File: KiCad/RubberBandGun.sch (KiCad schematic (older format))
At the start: 19 parts

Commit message: wiring for solenoid & move to pin 8
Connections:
- wire segments 120 -> 124
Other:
- note added: "Barrel Black Gnd\n Solenoid"
- note added: "Barrel White +5V\n Solenoid"
- note added: "D08 = Barrel (Yellow)\n grounded = closed"
- note added: "D13 = Solenoid\n (Blue)"
- note removed: "D09 = Barrel\n grounded = closed"
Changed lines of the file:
@@
 D07 = Red
 Text Notes 2200 2900 0    59   ~ 0
-D09 = Barrel\n    grounded = closed
+D08 = Barrel (Yellow)\n    grounded = closed
 $Comp
 L switches:SW_SPST SW?
@@
 	0    -1   -1   0
 $EndComp
-Text Notes 4850 5600 0    59   ~ 0
-D09 = Barrel\n    grounded = closed
+Text Notes 7250 4200 0    59   ~ 0
+Barrel White +5V\n    Solenoid
 $Comp
 L mdoLibrary:YX5200 A?
@@
 	4400 1100 4400 950
 Connection ~ 4400 950
-Wire Wire Line
-	4400 1400 4400 2800
 Wire Notes Line
 	7650 4450 7650 4750
@@
 Wire Wire Line
 	5350 3700 5350 3100
-Wire Wire Line
-	5350 2800 4400 2800
-Connection ~ 4400 2800
 Connection ~ 4200 6400
 Wire Wire Line
@@
 	7400 4500 7650 4500
 Wire Wire Line
-	7650 4500 7650 4700
+	7650 4500 7650 4600
 Wire Wire Line
 	7650 4700 7400 4700
@@
 Wire Wire Line
 	7050 6400 4800 6400
-Wire Wire Line
-	4400 2800 4400 4500
 Wire Wire Line
 	4200 6400 4000 6400
@@
 	1    0    0    -1
 $EndComp
+Wire Wire Line
+	4400 1400 4400 2700
+Wire Wire Line
+	5350 2700 4400 2700
+Connection ~ 4400 2700
+Wire Wire Line
+	4400 2700 4400 4500
+Text Notes 6600 3100 0    59   ~ 0
+D13 = Solenoid\n   (Blue)
+Text Notes 7250 5850 0    59   ~ 0
+Barrel Black Gnd\n    Solenoid
+Wire Wire Line
+	6550 3100 7200 3100
+Wire Wire Line
+	7200 3100 7200 4600
+Wire Wire Line
+	7200 4600 7650 4600
+Connection ~ 7650 4600
+Wire Wire Line
+	7650 4600 7650 4700
 $EndSCHEMATC

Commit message: latest schematic updates
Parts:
- added R?: 1.6K, symbol Device:R
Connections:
- wire segments 124 -> 128
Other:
- note added: "Barrel White +7.4V\n Solenoid"
- note added: "USB Breakout\n Black - GND\n White - +7.4 V\n Blue - Trig (HI = active)\n Yellow - Sense (GND = cnct)"
- note added: "Yes - connect GND"
- note removed: "Barrel White +5V\n Solenoid"
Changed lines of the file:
@@
 Sheet 1 2
 Title "FOOF Rubber Band Gun"
-Date "2020-01-30"
+Date "2020-03-14"
 Rev "---"
 Comp ""
@@
 F 3 "" H 2050 4450 60  0001 C CNN
 	1    2050 4450
-	1    0    0    -1
-$EndComp
-$Comp
-L mdoLibrary:UBEC #J0102
-U 1 1 5A459D02
-P 2050 6250
-F 0 "#J0102" H 2050 6250 60  0000 C CNN
-F 1 "UBEC" H 2050 6350 60  0000 C CNN
-F 2 "" H 2050 6250 60  0001 C CNN
-F 3 "" H 2050 6250 60  0001 C CNN
-	1    2050 6250
-	1    0    0    -1
-$EndComp
-$Comp
-L power:GND #PWR0103
-U 1 1 5A45A4D2
-P 1250 6950
-F 0 "#PWR0103" H 1250 6700 50  0001 C CNN
-F 1 "GND" H 1250 6800 50  0000 C CNN
-F 2 "" H 1250 6950 50  0001 C CNN
-F 3 "" H 1250 6950 50  0001 C CNN
-	1    1250 6950
-	1    0    0    -1
-$EndComp
-$Comp
-L power:+12V #PWR0104
-U 1 1 5A45A52D
-P 1250 5550
-F 0 "#PWR0104" H 1250 5400 50  0001 C CNN
-F 1 "+12V" H 1250 5690 50  0000 C CNN
-F 2 "" H 1250 5550 50  0001 C CNN
-F 3 "" H 1250 5550 50  0001 C CNN
-	1    1250 5550
 	1    0    0    -1
 $EndComp
@@
 Text Notes 7950 4850 3    118  ~ 0
 solenoid\ndriver
-Text Notes 900  3500 0    118  ~ 0
+Text Notes 1450 3850 0    118  ~ 0
 7.4 Volts
 $Comp
@@
 	0    -1   -1   0
 $EndComp
-Text Notes 7250 4200 0    59   ~ 0
-Barrel White +5V\n    Solenoid
+Text Notes 7450 4150 0    59   ~ 0
+Barrel White +7.4V\n    Solenoid
 $Comp
 L mdoLibrary:YX5200 A?
@@
 	1    0    0    -1
 $EndComp
-Connection ~ 3050 6400
-Wire Wire Line
-	1250 6000 1250 5550
-Wire Wire Line
-	1550 6000 1250 6000
-Wire Wire Line
-	1250 6400 1250 6950
-Wire Wire Line
-	1550 6400 1250 6400
 Wire Wire Line
 	9850 6400 8150 6400
 Wire Wire Line
-	3050 4600 3050 6400
+	3050 4600 3050 4900
 Wire Wire Line
 	2750 4600 3050 4600
@@
 	1250 4200 1550 4200
 Wire Wire Line
-	1250 3850 1250 4200
+	1250 3850 1250 3950
 Wire Wire Line
 	1250 4600 1550 4600
 Wire Wire Line
-	1250 4950 1250 4600
+	1250 4950 1250 4900
 Wire Wire Line
 	3200 4200 2750 4200
@@
 Connection ~ 4000 2500
 Wire Wire Line
-	2750 6000 9950 6000
-Wire Wire Line
 	9950 6000 9950 1800
 Wire Wire Line
-	6550 2000 7400 2000
-Connection ~ 7400 2000
+	6550 2000 6950 2000
 Wire Wire Line
 	4200 1100 4200 950
@@
 	4750 3900 4750 950
 Connection ~ 4750 950
-Wire Wire Line
-	7400 950  7400 2000
 Connection ~ 4600 950
 Wire Wire Line
@@
 Wire Wire Line
 	4600 1400 7600 1400
-Connection ~ 7400 950
 Wire Wire Line
 	7850 2150 7600 2150
@@
 	9350 1500 4950 1500
 Wire Wire Line
-	3050 6400 2750 6400
-Wire Wire Line
 	3400 6400 3050 6400
 Wire Wire Line
@@
 	4000 2500 4000 4100
 Wire Wire Line
-	7400 2000 7400 4500
-Wire Wire Line
 	4200 950  4400 950
 Wire Wire Line
@@
 	4800 6400 4200 6400
 Wire Wire Line
-	4750 950  7400 950
+	4750 950  6950 950
 Wire Wire Line
 	4600 950  4750 950
@@
 Wire Wire Line
 	7600 2250 7600 2450
-Wire Wire Line
-	7400 950  9050 950
 Wire Wire Line
 	9200 2250 9200 2350
@@
 	6550 3100 7200 3100
 Wire Wire Line
-	7200 3100 7200 4600
-Wire Wire Line
 	7200 4600 7650 4600
 Connection ~ 7650 4600
 Wire Wire Line
 	7650 4600 7650 4700
+Wire Wire Line
+	7200 3100 7200 3300
+Wire Wire Line
+	7200 3600 7200 4600
+$Comp
+L Device:R R?
+U 1 1 5E6E688B
+P 7200 3450
+F 0 "R?" V 7280 3450 50  0000 C CNN
+F 1 "1.6K" V 7200 3450 50  0000 C CNN
+F 2 "" V 7130 3450 50  0001 C CNN
+F 3 "" H 7200 3450 50  0001 C CNN
+	1    7200 3450
+	1    0    0    -1
+$EndComp
+Wire Wire Line
+	3200 4200 3200 6000
+Connection ~ 3200 4200
+Wire Wire Line
+	3200 6000 9950 6000
+Wire Wire Line
+	1250 4900 3050 4900
+Connection ~ 1250 4900
+Wire Wire Line
+	1250 4900 1250 4600
+Connection ~ 3050 4900
+Wire Wire Line
+	3050 4900 3050 6400
+Text Notes 1750 5000 0    59   ~ 0
+Yes - connect GND
+Wire Wire Line
+	6950 950  6950 2000
+Connection ~ 6950 950
+Wire Wire Line
+	6950 950  9050 950
+Wire Wire Line
+	1250 3950 1400 3950
+Wire Wire Line
+	1400 3950 1400 750
+Wire Wire Line
+	1400 750  7400 750
+Wire Wire Line
+	7400 750  7400 4500
+Connection ~ 1250 3950
+Wire Wire Line
+	1250 3950 1250 4200
+Text Notes 8300 4800 0    59   ~ 0
+USB Breakout\n   Black - GND\n   White - +7.4 V\n   Blue - Trig (HI = active)\n   Yellow - Sense (GND = cnct)
 $EndSCHEMATC

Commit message: add solenoid circuit
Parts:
- removed L?: L, symbol Device:L
- removed R?: 10K, symbol Device:R
- removed SW?: SW_SPST, symbol switches:SW_SPST
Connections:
- net labels added: Black, Blue, White, Yellow
- wire segments 128 -> 106
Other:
- note removed: "Barrel Black Gnd\n Solenoid"
- note removed: "Barrel White +7.4V\n Solenoid"
- note removed: "USB Breakout\n Black - GND\n White - +7.4 V\n Blue - Trig (HI = active)\n Yellow - Sense (GND = cnct)"
- note removed: "solenoid\ndriver"

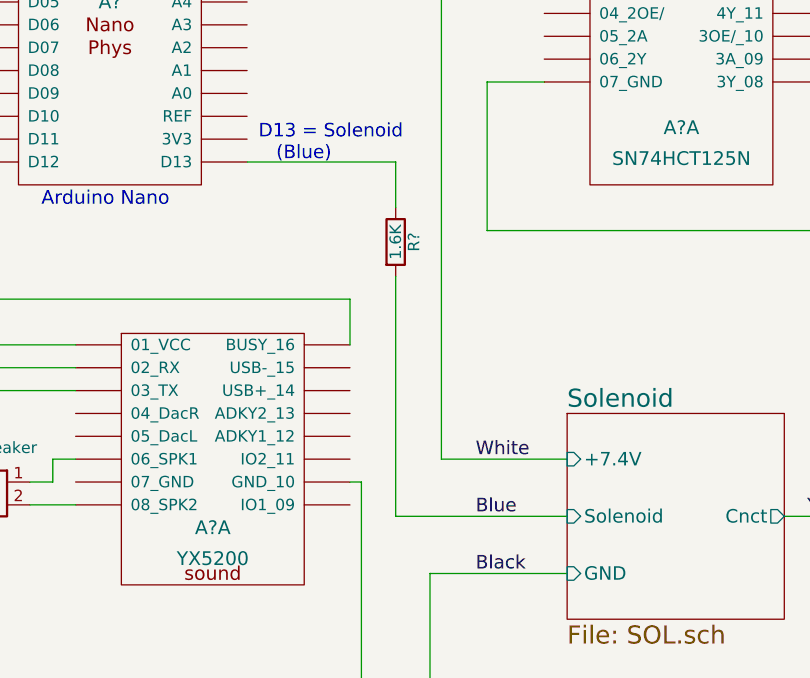
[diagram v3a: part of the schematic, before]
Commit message: small change to schematic
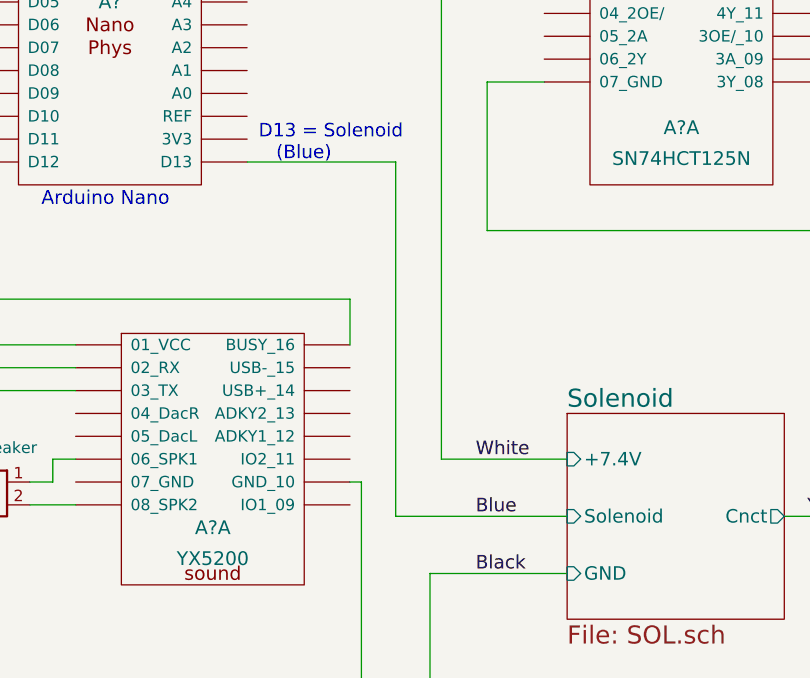
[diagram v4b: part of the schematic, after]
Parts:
- removed R?: 1.6K, symbol Device:R
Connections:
- wire segments 106 -> 105
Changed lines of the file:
@@
 Sheet 1 2
 Title "FOOF Rubber Band Gun"
-Date "2020-03-14"
+Date "2020-04-02"
 Rev "---"
 Comp ""
@@
 Wire Wire Line
 	6550 3100 7200 3100
-Wire Wire Line
-	7200 3100 7200 3300
-$Comp
-L Device:R R?
-U 1 1 5E6E688B
-P 7200 3450
-F 0 "R?" V 7280 3450 50  0000 C CNN
-F 1 "1.6K" V 7200 3450 50  0000 C CNN
-F 2 "" V 7130 3450 50  0001 C CNN
-F 3 "" H 7200 3450 50  0001 C CNN
-	1    7200 3450
-	1    0    0    -1
-$EndComp
 Wire Wire Line
 	3200 4200 3200 6000
@@
 $EndSheet
 Wire Wire Line
-	7200 3600 7200 4650
-Wire Wire Line
 	4200 6400 7050 6400
 Wire Wire Line
@@
 Wire Wire Line
 	4400 950  4750 950
+Wire Wire Line
+	7200 3100 7200 4650
 $EndSCHEMATC

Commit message: update schematic to show power and USB details
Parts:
- added SW?: ToggleSW, symbol switches:SW_SPST
- added U?: SolenoidDriver, symbol mdoLibrary:SolenoidDriver
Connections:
- net labels added: +8V
- net labels removed: +12V, Black, Blue, White, Yellow
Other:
- note added: "8.3 Volts"
- note added: "Black"
- note added: "Blue"
- note added: "White"
- note added: "Yellow"
- note removed: "7.4 Volts"
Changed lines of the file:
@@
 $Descr A 11000 8500
 encoding utf-8
-Sheet 1 2
+Sheet 1 1
 Title "FOOF Rubber Band Gun"
-Date "2020-04-02"
+Date "2020-07-13"
 Rev "---"
 Comp ""
@@
 Comment4 ""
 $EndDescr
-$Comp
-L power:+12V #PWR0101
-U 1 1 5A3DEBB7
-P 1250 3850
-F 0 "#PWR0101" H 1250 3700 50  0001 C CNN
-F 1 "+12V" H 1250 3990 50  0000 C CNN
-F 2 "" H 1250 3850 50  0001 C CNN
-F 3 "" H 1250 3850 50  0001 C CNN
-	1    1250 3850
-	1    0    0    -1
-$EndComp
 $Comp
 L power:GND #PWR0102
@@
 $EndComp
 Text Notes 1450 3850 0    118  ~ 0
-7.4 Volts
+8.3 Volts
 $Comp
 L Device:R R?
@@
 	2750 4600 3050 4600
 Wire Wire Line
-	1250 4200 1550 4200
-Wire Wire Line
-	1250 3850 1250 3950
-Wire Wire Line
 	1250 4600 1550 4600
 Wire Wire Line
@@
 	6950 950  9050 950
 Wire Wire Line
-	1250 3950 1400 3950
-Wire Wire Line
-	1400 3950 1400 750
-Wire Wire Line
 	1400 750  7400 750
 Wire Wire Line
-	7400 750  7400 4400
-Connection ~ 1250 3950
-Wire Wire Line
-	1250 3950 1250 4200
-Text Label 7550 4400 0    59   ~ 0
-White
-$Sheet
-S 7950 4200 950  900
-U 5B063CC5
-F0 "Solenoid" 79
-F1 "SOL.sch" 79
-F2 "+7.4V" I L 7950 4400 59
-F3 "GND" I L 7950 4900 59
-F4 "Solenoid" I L 7950 4650 59
-F5 "Cnct" O R 8900 4650 59
-$EndSheet
+	7400 750  7400 4300
 Wire Wire Line
 	4200 6400 7050 6400
 Wire Wire Line
-	7050 6400 7350 6400
-Wire Wire Line
-	7400 4400 7950 4400
-Wire Wire Line
-	7200 4650 7950 4650
-Wire Wire Line
-	7350 6400 7350 4900
-Wire Wire Line
-	7350 4900 7950 4900
-Connection ~ 7350 6400
-Wire Wire Line
-	7350 6400 9850 6400
-Wire Wire Line
-	4400 5500 9750 5500
-Wire Wire Line
-	9750 5500 9750 4650
-Wire Wire Line
 	4400 2700 4400 5500
-Wire Wire Line
-	8900 4650 9750 4650
-Text Label 7550 4900 0    59   ~ 0
-Black
-Text Label 7550 4650 0    59   ~ 0
-Blue
-Text Label 9000 4650 0    59   ~ 0
-Yellow
 $Comp
 L mdoLibrary:SN74HCT125N A?
@@
 	4400 950  4750 950
 Wire Wire Line
-	7200 3100 7200 4650
+	7200 3100 7200 4500
+Wire Wire Line
+	1400 750  1400 4200
+Wire Wire Line
+	1550 4200 1400 4200
+$Comp
+L power:+8V #PWR?
+U 1 1 5F0E58C5
+P 650 3950
+F 0 "#PWR?" H 650 3800 50  0001 C CNN
+F 1 "+8V" H 665 4123 50  0000 C CNN
+F 2 "" H 650 3950 50  0001 C CNN
+F 3 "" H 650 3950 50  0001 C CNN
+	1    650  3950
+	1    0    0    -1
+$EndComp
+Wire Wire Line
+	650  4200 650  3950
+$Comp
+L mdoLibrary:SolenoidDriver U?
+U 1 1 5F10689D
+P 9400 4100
+F 0 "U?" H 9400 4100 59  0001 C CNN
+F 1 "SolenoidDriver" H 9100 4100 59  0000 L CNN
+F 2 "" H 9400 4100 59  0001 C CNN
+F 3 "" H 9400 4100 59  0001 C CNN
+	1    9400 4100
+	1    0    0    -1
+$EndComp
+Wire Wire Line
+	4400 5500 7600 5500
+Wire Wire Line
+	7600 5500 7600 5000
+Wire Wire Line
+	7600 5000 8650 5000
+Wire Wire Line
+	7050 6400 7950 6400
+Wire Wire Line
+	7950 6400 7950 4850
+Wire Wire Line
+	7950 4850 8650 4850
+Connection ~ 7950 6400
+Wire Wire Line
+	7950 6400 9850 6400
+Wire Wire Line
+	8650 4300 7400 4300
+Wire Wire Line
+	8650 4500 7200 4500
+Text Notes 8300 4300 0    59   ~ 0
+White
+Text Notes 8300 4500 0    59   ~ 0
+Blue
+Text Notes 8300 4850 0    59   ~ 0
+Black
+Text Notes 8300 5000 0    59   ~ 0
+Yellow
+$Comp
+L switches:SW_SPST SW?
+U 1 1 5F12E089
+P 1000 4200
+F 0 "SW?" H 1000 4450 50  0001 C CNN
+F 1 "ToggleSW" H 1000 4344 50  0000 C CNN
+F 2 "" H 1000 4200 50  0001 C CNN
+F 3 "" H 1000 4200 50  0001 C CNN
+	1    1000 4200
+	1    0    0    -1
+$EndComp
+Wire Wire Line
+	650  4200 800  4200
+Wire Wire Line
+	1200 4200 1400 4200
+Connection ~ 1400 4200
 $EndSCHEMATC

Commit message: add LED ring wiring, clarify USB connection
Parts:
- removed U?: SolenoidDriver, symbol mdoLibrary:SolenoidDriver
- removed Z?: LEDring, symbol mdoLibrary:LEDring
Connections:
- net labels added: 5V, Black_GND, Blue_CTL, DIN, White_8V, Yellow_SENSE
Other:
- note added: "U\nS\nB"
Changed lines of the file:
@@
 $Descr A 11000 8500
 encoding utf-8
-Sheet 1 1
+Sheet 1 3
 Title "FOOF Rubber Band Gun"
-Date "2020-07-13"
+Date "2020-07-18"
 Rev "---"
 Comp ""
@@
 Wire Wire Line
 	9850 1800 9850 2550
-$Comp
-L mdoLibrary:LEDring Z?
-U 1 1 5A458774
-P 9900 1100
-F 0 "Z?" H 9900 1100 60  0000 C CNN
-F 1 "LEDring" H 9900 1250 60  0000 C CNN
-F 2 "" H 9900 1250 60  0001 C CNN
-F 3 "" H 9900 1250 60  0001 C CNN
-	1    9900 1100
-	1    0    0    -1
-$EndComp
 Wire Wire Line
 	4400 1400 4400 2700
@@
 Wire Wire Line
 	650  4200 650  3950
-$Comp
-L mdoLibrary:SolenoidDriver U?
-U 1 1 5F10689D
-P 9400 4100
-F 0 "U?" H 9400 4100 59  0001 C CNN
-F 1 "SolenoidDriver" H 9100 4100 59  0000 L CNN
-F 2 "" H 9400 4100 59  0001 C CNN
-F 3 "" H 9400 4100 59  0001 C CNN
-	1    9400 4100
-	1    0    0    -1
-$EndComp
 Wire Wire Line
 	4400 5500 7600 5500
@@
 	1200 4200 1400 4200
 Connection ~ 1400 4200
+Text Notes 8700 5000 0    157  ~ 31
+U\nS\nB
+$Sheet
+S 8950 4200 700  900
+U 5F12AD06
+F0 "Solenoid" 59
+F1 "Solenoid.sch" 59
+$EndSheet
+Text HLabel 8950 4300 2    59   Input ~ 0
+White_8V
+Text HLabel 8950 4500 2    59   Input ~ 0
+Blue_CTL
+Text HLabel 8950 4850 2    59   Input ~ 0
+Black_GND
+Text HLabel 8950 5000 2    59   Output ~ 0
+Yellow_SENSE
+$Sheet
+S 9500 900  850  900
+U 5F14546D
+F0 "LEDrings" 79
+F1 "LEDrings.sch" 0
+$EndSheet
+Text HLabel 9850 1800 1    59   Input ~ 0
+GND
+Text HLabel 9950 1800 1    59   Input ~ 0
+5V
+Text HLabel 10050 1800 1    59   Input ~ 0
+DIN
 $EndSCHEMATC
